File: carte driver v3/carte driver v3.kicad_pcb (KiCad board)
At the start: 2 copper layers, 96.8 x 34.8 mm, 49 parts, among them J1 UART CP, J10 STEPPER 2, J11 STEPPER 4, J2 UART BONUS, J3 conn 24v, J4 conn 5v, J5 ventilo, J6 STEPPER G, J7 STEPPER 1, J8 STEPPER 3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

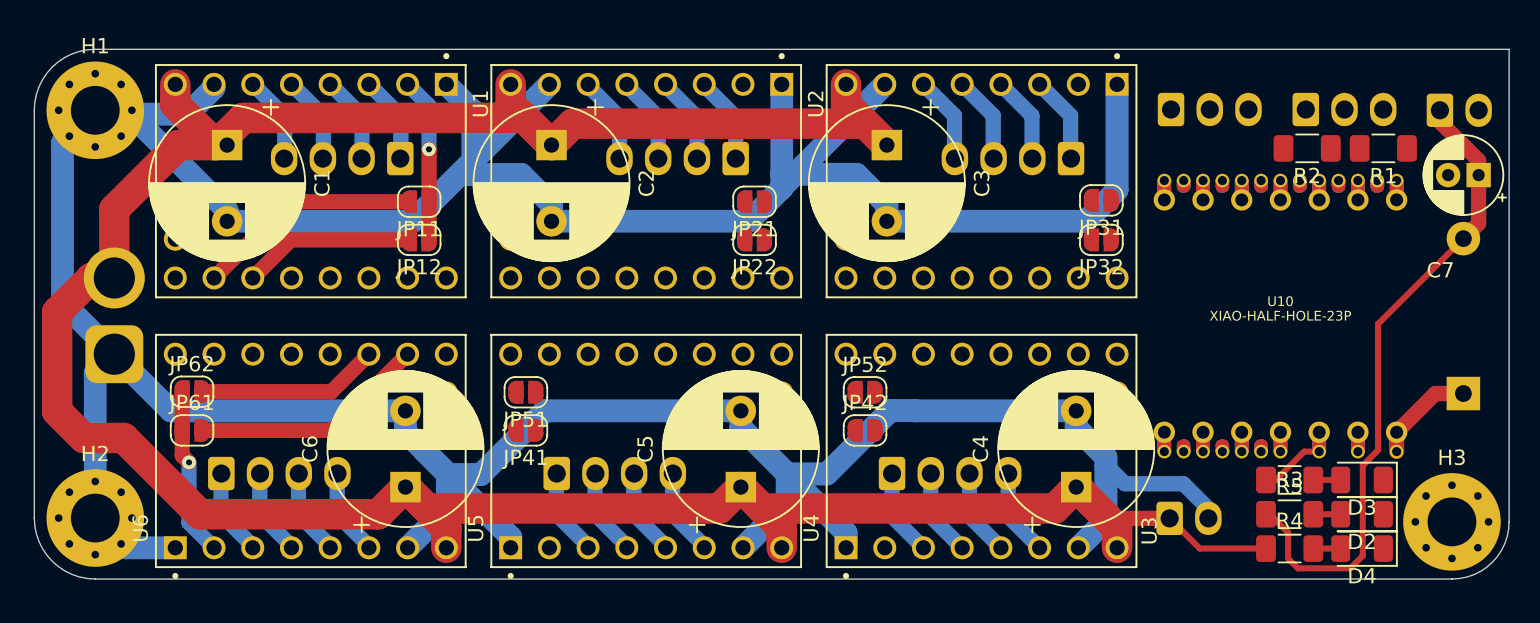
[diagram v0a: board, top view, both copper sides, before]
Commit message: v3 fin routage
on espere que c'est le cas
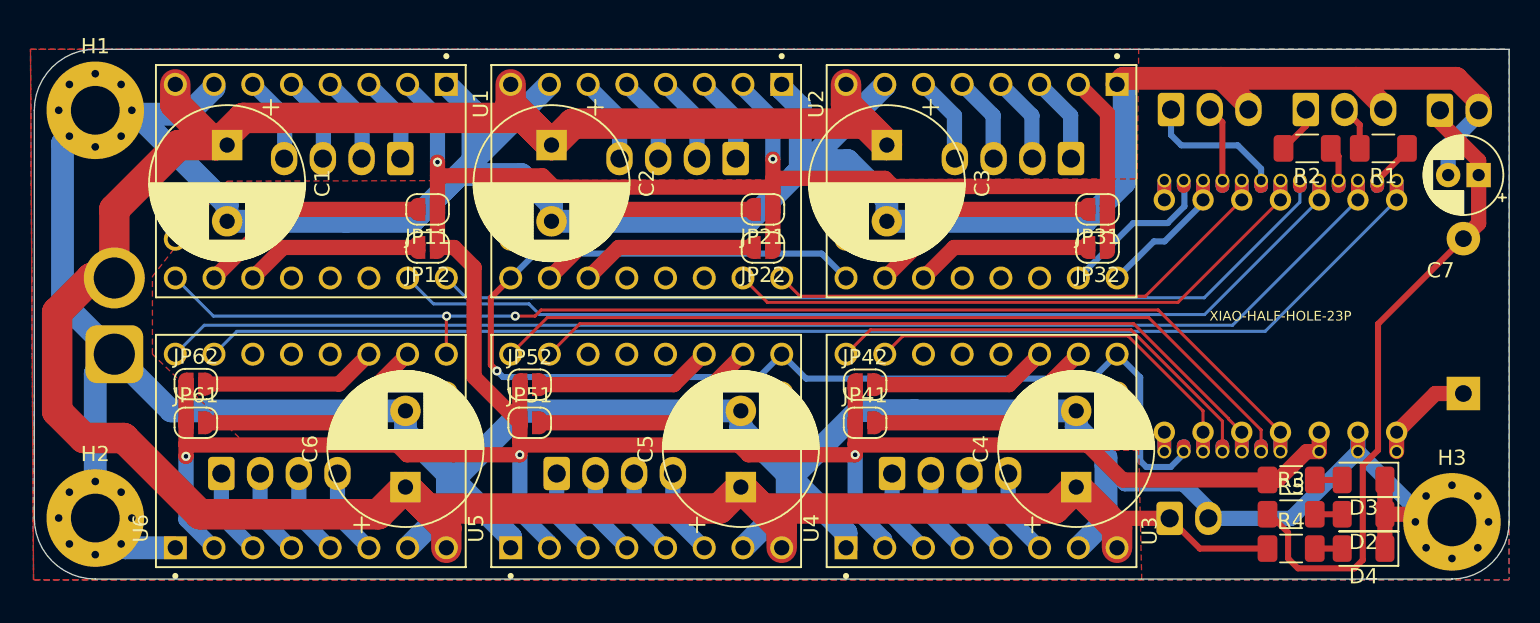
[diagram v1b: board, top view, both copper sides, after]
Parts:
- moved JP41 22.3 mm to (204.8, 99.0), turned to 0 degrees
- moved JP52 22.0 mm to (182.8, 96.5)
- moved JP42 3.00 mm to (204.8, 96.5)
- moved JP51 2.02 mm to (182.8, 99.0), turned to 0 degrees
- moved JP11 0.74 mm to (176.1, 85.0)
- moved JP12 0.74 mm to (176.1, 87.5)
- moved JP21 0.74 mm to (198.1, 85.0)
- moved JP22 0.74 mm to (198.1, 87.5)
- moved JP31 0.64 mm to (220.0, 85.0)
- moved JP32 0.56 mm to (220.0, 87.5)
- moved JP61 0.56 mm to (160.9, 99.0)
- moved JP62 0.56 mm to (160.9, 96.5)
- moved D2 0.10 mm to (237.5, 105.0)
- moved D3 0.10 mm to (237.5, 102.8)
- moved D4 0.10 mm to (237.5, 107.2)
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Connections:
- U10 pad 1: STEP 4 -> STEP 6
- U10 pad 17: unconnected-(U10-GPIO40_CAM_SDA/I2S_WS-Pad17) -> DIR 1
- U10 pad 18: unconnected-(U10-GPIO41_PDM_DATA/RX1-Pad18) -> RX
- U10 pad 19: DIR 3 -> TX
- U10 pad 2: DIR 4 -> DIR 6
- U10 pad 22: DIR 6 -> DIR 4
- U10 pad 4: DIR 1 -> STEP 2
- U10 pad 5: STEP 2 -> DIR 2
- U10 pad 6: DIR 2 -> DIR 3
- U10 pad 7: TX -> unconnected-(U10-U0TXD_D6/TX-Pad7)
- U10 pad 8: RX -> unconnected-(U10-U0RXD_D7/RX-Pad8)
- U10 pad 9: STEP 6 -> STEP 4
- U4 pad 16: EN M -> EN
- U6 pad 16: EN -> EN M
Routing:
- net +3.3V: track 27.4 -> 205.9 mm, vias 2 -> 5
- net EN: track 0.00 -> 84.1 mm, vias 0 -> 1
- net STEP 6: track 0.00 -> 83.0 mm
- net DIR 6: track 0.00 -> 83.0 mm
- net EN M: track 0.00 -> 80.8 mm, vias 0 -> 2
- net STEP 1: track 0.00 -> 65.2 mm
- net GND: track 288.3 -> 350.9 mm
- net DIR 1: track 0.00 -> 60.5 mm
- net DIR 5: track 0.00 -> 54.7 mm
- net STEP 5: track 0.00 -> 50.5 mm
- net STEP 2: track 0.00 -> 40.0 mm
- net DIR 2: track 0.00 -> 34.6 mm
- net DIR 4: track 0.00 -> 29.8 mm
- net STEP 4: track 0.00 -> 26.1 mm
- net Net-(JP21-B): track 0.00 -> 15.2 mm
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- added copper zone on F.Cu, net +24V
- added copper zone on B.Cu, net GND
- added copper zone on F.Cu, net GND

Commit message: v3
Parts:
- added kibuzzard-690E8D8B: G***, kibuzzard-690E8D8B, F.Cu at (234.5, 86.5)
- added kibuzzard-690E8DC3: G***, kibuzzard-690E8DC3, F.Cu at (239.6, 86.5)
- added kibuzzard-690E8DDF: G***, kibuzzard-690E8DDF, F.Cu at (232.0, 86.5)
- added kibuzzard-690E8E20: G***, kibuzzard-690E8E20, F.Cu at (225.7, 85.1)
- added kibuzzard-690E8E58: G***, kibuzzard-690E8E58, F.Cu at (229.5, 97.5)
- added kibuzzard-690E8E91: G***, kibuzzard-690E8E91, F.Cu at (227.0, 97.5)
- added kibuzzard-690E8EB4: G***, kibuzzard-690E8EB4, F.Cu at (233.3, 84.9)
- added kibuzzard-690E8ECA: G***, kibuzzard-690E8ECA, F.Cu at (237.1, 86.3)
- added kibuzzard-690E8EDD: G***, kibuzzard-690E8EDD, F.Cu at (229.5, 86.3)
- added kibuzzard-690E8EED: G***, kibuzzard-690E8EED, F.Cu at (226.9, 86.3)
- added kibuzzard-690E8EFE: G***, kibuzzard-690E8EFE, F.Cu at (230.7, 99.1)
- added kibuzzard-690E8F10: G***, kibuzzard-690E8F10, F.Cu at (228.2, 99.1)
- added kibuzzard-690E8F27: G***, kibuzzard-690E8F27, F.Cu at (225.7, 99.7)
- added kibuzzard-690E8F3D: G***, kibuzzard-690E8F3D, F.Cu at (232.0, 97.9)
- added kibuzzard-690E90CC: G***, kibuzzard-690E90CC, F.Cu at (228.2, 84.3)
- added kibuzzard-690E90D9: G***, kibuzzard-690E90D9, F.Cu at (230.7, 84.3)
- added kibuzzard-690E90FE: G***, kibuzzard-690E90FE, F.Cu at (235.8, 84.7)
- added kibuzzard-690E9105: G***, kibuzzard-690E9105, F.Cu at (238.4, 84.7)
- added kibuzzard-690E924D: G***, kibuzzard-690E924D, B.Cu at (227.4, 75.1)
- added kibuzzard-690E925F: G***, kibuzzard-690E925F, B.Cu at (236.2, 75.1)
- added kibuzzard-690E9271: G***, kibuzzard-690E9271, B.Cu at (243.7, 75.2)
- added kibuzzard-690E929D: G***, kibuzzard-690E929D, B.Cu at (152.4, 92.0)
- added kibuzzard-690E92EA: G***, kibuzzard-690E92EA, B.Cu at (226.0, 108.6)
- added kibuzzard-690E93A6: G***, kibuzzard-690E93A6, F.Cu at (237.4, 102.0)
- added kibuzzard-690E93B3: G***, kibuzzard-690E93B3, F.Cu at (237.4, 104.2)
- added kibuzzard-690E93BF: G***, kibuzzard-690E93BF, F.Cu at (237.4, 106.5)
- added kibuzzard-690E9406: G***, kibuzzard-690E9406, F.Cu at (232.7, 104.5)
- added kibuzzard-690E9406: G***, kibuzzard-690E9406, F.Cu at (232.7, 102.2)
- added kibuzzard-690E9406: G***, kibuzzard-690E9406, F.Cu at (238.8, 80.5)
- added kibuzzard-690E9406: G***, kibuzzard-690E9406, F.Cu at (233.8, 80.5)
- added kibuzzard-690E9406: G***, kibuzzard-690E9406, F.Cu at (232.7, 106.7)
- added kibuzzard-690E943A: G***, kibuzzard-690E943A, F.Cu at (232.7, 103.2)
- added kibuzzard-690E943A: G***, kibuzzard-690E943A, F.Cu at (232.7, 105.5)
- added kibuzzard-690E943A: G***, kibuzzard-690E943A, F.Cu at (238.8, 81.5)
- added kibuzzard-690E943A: G***, kibuzzard-690E943A, F.Cu at (232.7, 107.8)
- added kibuzzard-690E943A: G***, kibuzzard-690E943A, F.Cu at (233.8, 81.5)
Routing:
- net EN: track 84.1 -> 81.1 mm
- net RX: track 9.28 -> 8.30 mm

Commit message: Fin v3 avec annotation
ça peut partir en prod
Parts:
- added G***: LOGO, LOGO, B.Cu at (192.5, 97.5)
- added kibuzzard-69108723: G***, kibuzzard-69108723, B.Cu at (210.3, 99.0)
- added kibuzzard-6910874F: G***, kibuzzard-6910874F, B.Cu at (166.5, 99.0)
- added kibuzzard-6910875C: G***, kibuzzard-6910875C, B.Cu at (188.4, 99.0)
- added kibuzzard-69108793: G***, kibuzzard-69108793, B.Cu at (170.5, 85.0)
- added kibuzzard-691087A0: G***, kibuzzard-691087A0, B.Cu at (192.4, 85.0)
- added kibuzzard-691087AC: G***, kibuzzard-691087AC, B.Cu at (214.3, 85.0)
- kibuzzard-690E8D8B, kibuzzard-690E8DC3, kibuzzard-690E8DDF, kibuzzard-690E8E20, kibuzzard-690E8E58, kibuzzard-690E8E91, kibuzzard-690E8EB4, kibuzzard-690E8ECA, kibuzzard-690E8EDD, kibuzzard-690E8EED, kibuzzard-690E8EFE, kibuzzard-690E8F10, kibuzzard-690E8F27, kibuzzard-690E8F3D, kibuzzard-690E90CC, kibuzzard-690E90D9, kibuzzard-690E90FE, kibuzzard-690E9105: moved to B.Cu
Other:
- board text added: "By Oscar Yosh GRIVELET"
- board text added: "Carte_Driver 2026_V2"

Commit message: pareil
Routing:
- net GND: track 350.9 -> 361.1 mm
- removed copper zone on F.Cu, net GND
